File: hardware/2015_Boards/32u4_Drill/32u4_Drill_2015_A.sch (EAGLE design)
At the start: 25 parts, among them U2 XBEE-1B3

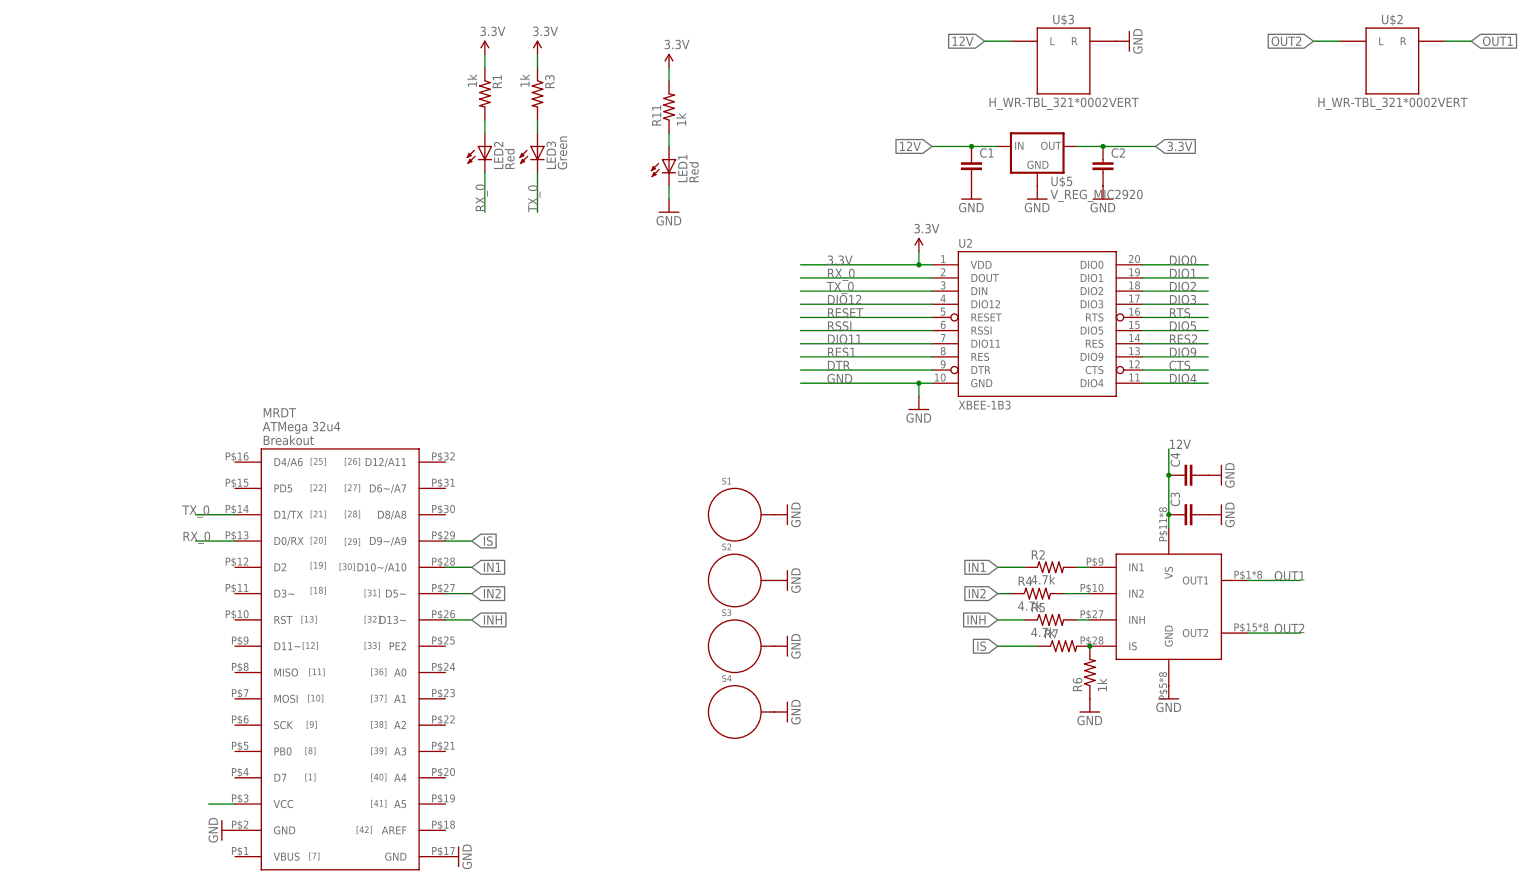
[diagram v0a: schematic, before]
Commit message: Update some Capacitor Values
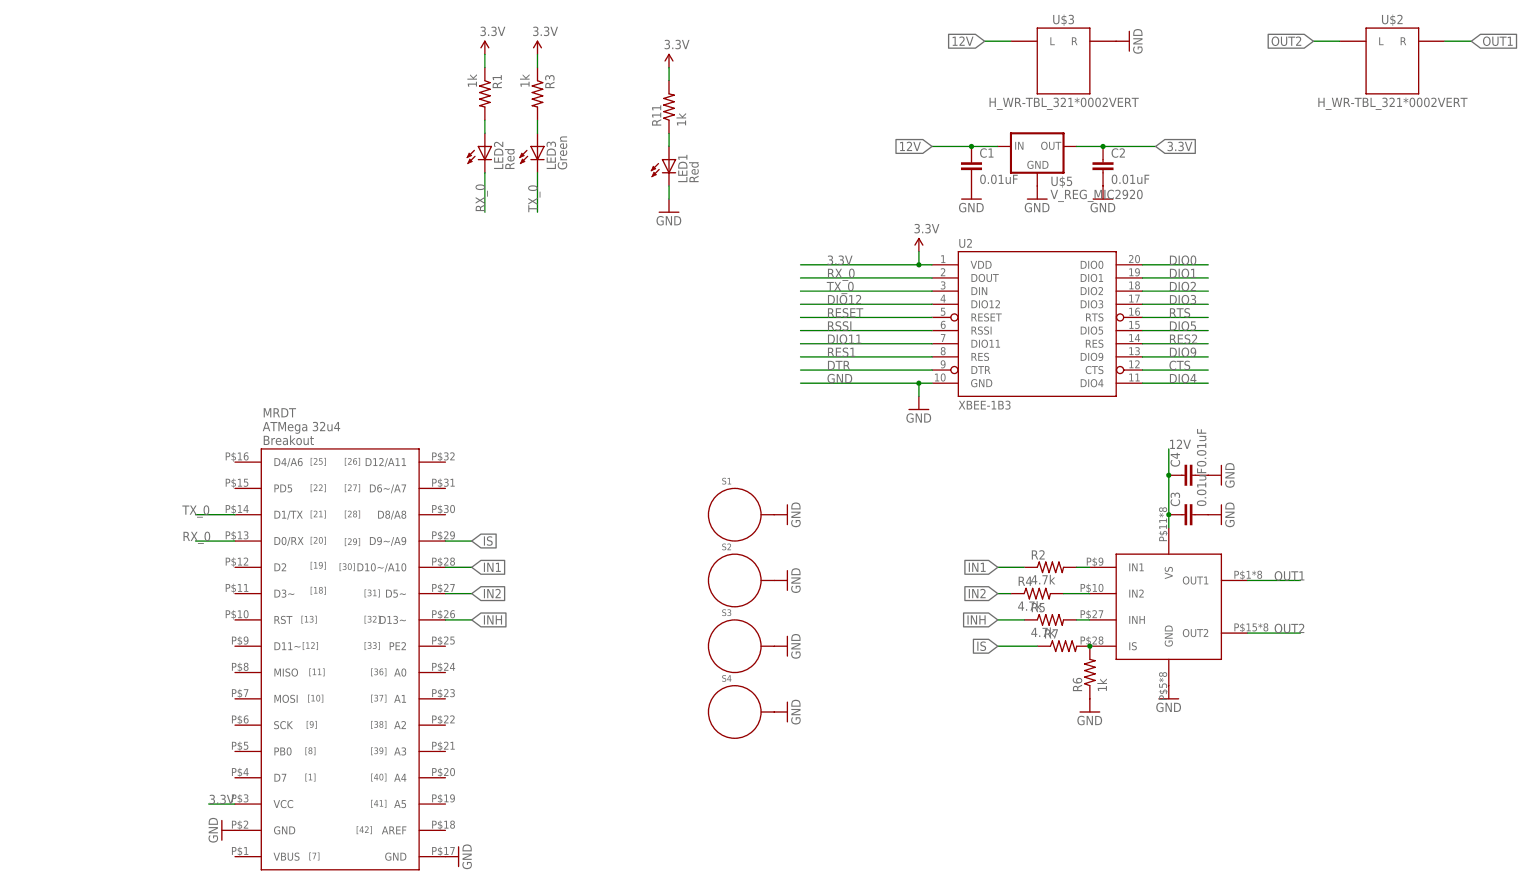
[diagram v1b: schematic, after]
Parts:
- C1, C2, C3, C4: value (none) -> 0.01uF
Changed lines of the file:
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@@
 <?xml version="1.0" encoding="utf-8"?>
 <!DOCTYPE eagle SYSTEM "eagle.dtd">
-<eagle version="6.6.0">
+<eagle version="6.5.0">
 <drawing>
 <settings>
@@
 <part name="U$4" library="MRDT-2015-General" deviceset="BTM7752G" device=""/>
 <part name="GND10" library="SparkFun" deviceset="GND" device=""/>
-<part name="C1" library="SparkFun-Passives" deviceset="CAP" device="1206"/>
-<part name="C2" library="SparkFun-Passives" deviceset="CAP" device="1206"/>
+<part name="C1" library="SparkFun-Passives" deviceset="CAP" device="1206" value="0.01uF"/>
+<part name="C2" library="SparkFun-Passives" deviceset="CAP" device="1206" value="0.01uF"/>
 <part name="GND11" library="SparkFun" deviceset="GND" device=""/>
 <part name="GND12" library="SparkFun" deviceset="GND" device=""/>
@@
 <part name="GND13" library="SparkFun" deviceset="GND" device=""/>
 <part name="R7" library="SparkFun-Passives" deviceset="RESISTOR" device="1206"/>
-<part name="C3" library="SparkFun-Passives" deviceset="CAP" device="1206"/>
-<part name="C4" library="SparkFun-Passives" deviceset="CAP" device="1206"/>
+<part name="C3" library="SparkFun-Passives" deviceset="CAP" device="1206" value="0.01uF"/>
+<part name="C4" library="SparkFun-Passives" deviceset="CAP" device="1206" value="0.01uF"/>
 <part name="GND14" library="SparkFun" deviceset="GND" device=""/>
 <part name="GND15" library="SparkFun" deviceset="GND" device=""/>
@@
 <pinref part="U$1" gate="G$1" pin="VCC"/>
 <wire x1="0" y1="15.24" x2="5.08" y2="15.24" width="0.1524" layer="91"/>
-</segment>
-<segment>
+<label x="0" y="15.24" size="1.778" layer="95"/>
+</segment>
+<segment>

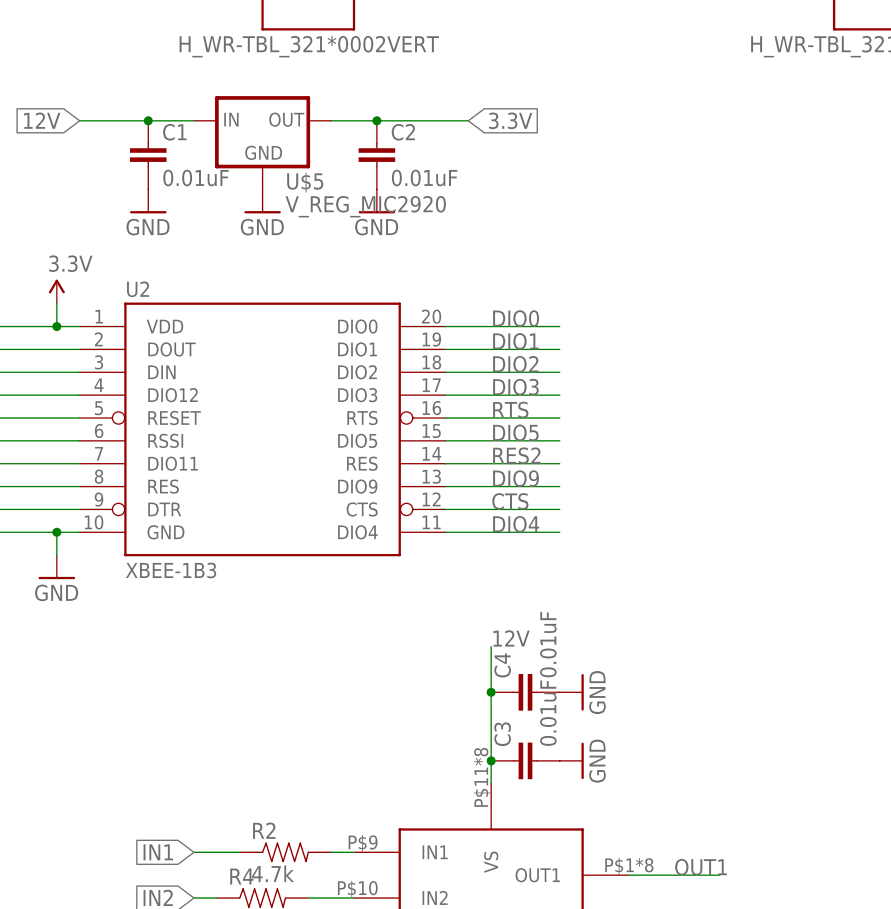
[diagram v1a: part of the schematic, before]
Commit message: Added a beefy capacitor because the datasheet told me too
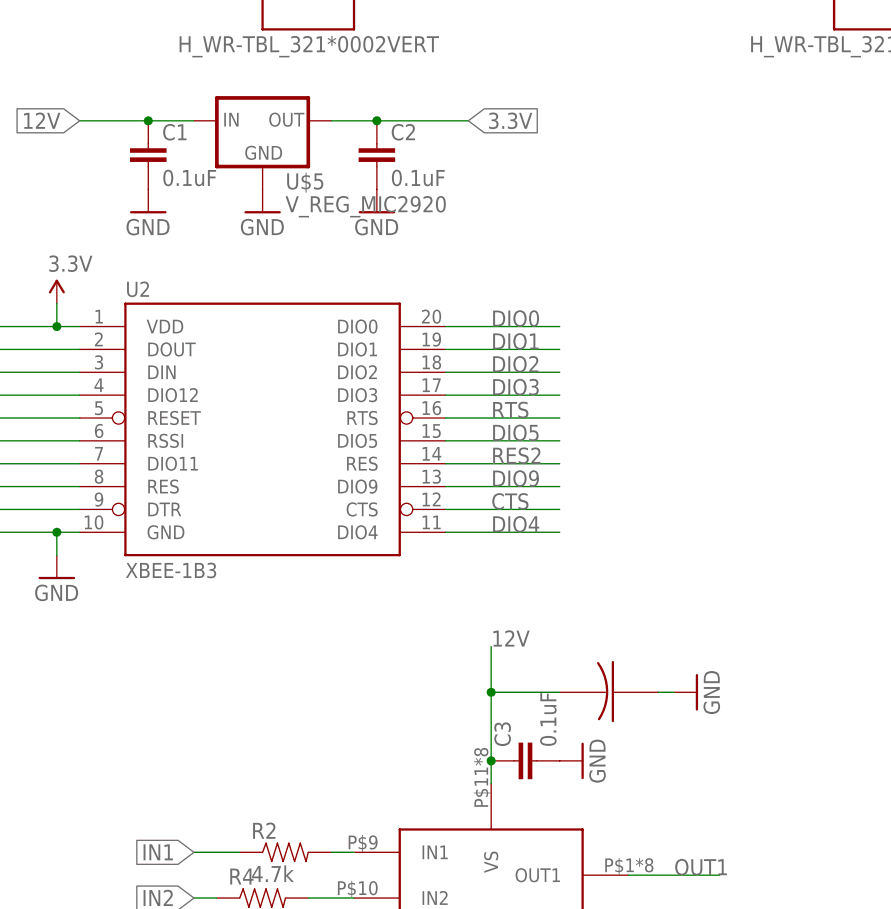
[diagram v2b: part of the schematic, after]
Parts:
- removed C4: 0.01uF, SparkFun-Passives:CAP1206
- added U$6: 100UF-ELECTRO-CAP, New:100UF-ELECTRO-CAP
- C1, C2, C3: value 0.01uF -> 0.1uF
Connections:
- net 12V: now also U$6.POS; no longer C4.1
- net GND: no longer C4.2
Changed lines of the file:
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@@
 <setting verticaltext="up"/>
 </settings>
-<grid distance="0.1" unitdist="inch" unit="inch" style="lines" multiple="1" display="no" altdistance="0.01" altunitdist="inch" altunit="inch"/>
+<grid distance="0.01" unitdist="inch" unit="inch" style="lines" multiple="1" display="no" altdistance="0.01" altunitdist="inch" altunit="inch"/>
 <layers>
 <layer number="1" name="Top" color="4" fill="1" visible="no" active="no"/>
 <layer number="2" name="Route2" color="1" fill="3" visible="no" active="no"/>
+<layer number="3" name="Route3" color="4" fill="3" visible="no" active="no"/>
+<layer number="4" name="Route4" color="1" fill="4" visible="no" active="no"/>
+<layer number="5" name="Route5" color="4" fill="4" visible="no" active="no"/>
+<layer number="6" name="Route6" color="1" fill="8" visible="no" active="no"/>
+<layer number="7" name="Route7" color="4" fill="8" visible="no" active="no"/>
+<layer number="8" name="Route8" color="1" fill="2" visible="no" active="no"/>
+<layer number="9" name="Route9" color="4" fill="2" visible="no" active="no"/>
+<layer number="10" name="Route10" color="1" fill="7" visible="no" active="no"/>
+<layer number="11" name="Route11" color="4" fill="7" visible="no" active="no"/>
+<layer number="12" name="Route12" color="1" fill="5" visible="no" active="no"/>
+<layer number="13" name="Route13" color="4" fill="5" visible="no" active="no"/>
+<layer number="14" name="Route14" color="1" fill="6" visible="no" active="no"/>
 <layer number="15" name="Route15" color="4" fill="6" visible="no" active="no"/>
 <layer number="16" name="Bottom" color="1" fill="1" visible="no" active="no"/>
@@
 <part name="U$4" library="MRDT-2015-General" deviceset="BTM7752G" device=""/>
 <part name="GND10" library="SparkFun" deviceset="GND" device=""/>
-<part name="C1" library="SparkFun-Passives" deviceset="CAP" device="1206" value="0.01uF"/>
-<part name="C2" library="SparkFun-Passives" deviceset="CAP" device="1206" value="0.01uF"/>
+<part name="C1" library="SparkFun-Passives" deviceset="CAP" device="1206" value="0.1uF"/>
+<part name="C2" library="SparkFun-Passives" deviceset="CAP" device="1206" value="0.1uF"/>
 <part name="GND11" library="SparkFun" deviceset="GND" device=""/>
 <part name="GND12" library="SparkFun" deviceset="GND" device=""/>
@@
 <part name="GND13" library="SparkFun" deviceset="GND" device=""/>
 <part name="R7" library="SparkFun-Passives" deviceset="RESISTOR" device="1206"/>
-<part name="C3" library="SparkFun-Passives" deviceset="CAP" device="1206" value="0.01uF"/>
-<part name="C4" library="SparkFun-Passives" deviceset="CAP" device="1206" value="0.01uF"/>
+<part name="C3" library="SparkFun-Passives" deviceset="CAP" device="1206" value="0.1uF"/>
 <part name="GND14" library="SparkFun" deviceset="GND" device=""/>
 <part name="GND15" library="SparkFun" deviceset="GND" device=""/>
+<part name="U$6" library="New" deviceset="100UF-ELECTRO-CAP" device=""/>
 </parts>
 <sheets>
@@
 <instance part="R7" gate="G$1" x="165.1" y="45.72"/>
 <instance part="C3" gate="G$1" x="190.5" y="71.12" rot="R90"/>
-<instance part="C4" gate="G$1" x="190.5" y="78.74" rot="R90"/>
-<instance part="GND14" gate="1" x="195.58" y="78.74" rot="R90"/>
+<instance part="GND14" gate="1" x="208.28" y="78.74" rot="R90"/>
 <instance part="GND15" gate="1" x="195.58" y="71.12" rot="R90"/>
+<instance part="U$6" gate="G$1" x="220.98" y="66.04"/>
 </instances>
 <busses>
@@
 </segment>
 <segment>
-<pinref part="C4" gate="G$1" pin="2"/>
-<pinref part="GND14" gate="1" pin="GND"/>
-</segment>
-<segment>
 <pinref part="C3" gate="G$1" pin="2"/>
 <pinref part="GND15" gate="1" pin="GND"/>
+</segment>
+<segment>
+<pinref part="GND14" gate="1" pin="GND"/>
+<wire x1="205.74" y1="78.74" x2="203.962" y2="78.74" width="0.1524" layer="91"/>
 </segment>
 </net>
@@
 <wire x1="185.42" y1="71.12" x2="185.42" y2="78.74" width="0.1524" layer="91"/>
 <junction x="185.42" y="71.12"/>
-<pinref part="C4" gate="G$1" pin="1"/>
+<pinref part="U$6" gate="G$1" pin="POS"/>
 <wire x1="185.42" y1="78.74" x2="185.42" y2="83.82" width="0.1524" layer="91"/>
+<wire x1="193.04" y1="78.74" x2="185.42" y2="78.74" width="0.1524" layer="91"/>
 <junction x="185.42" y="78.74"/>
 </segment>

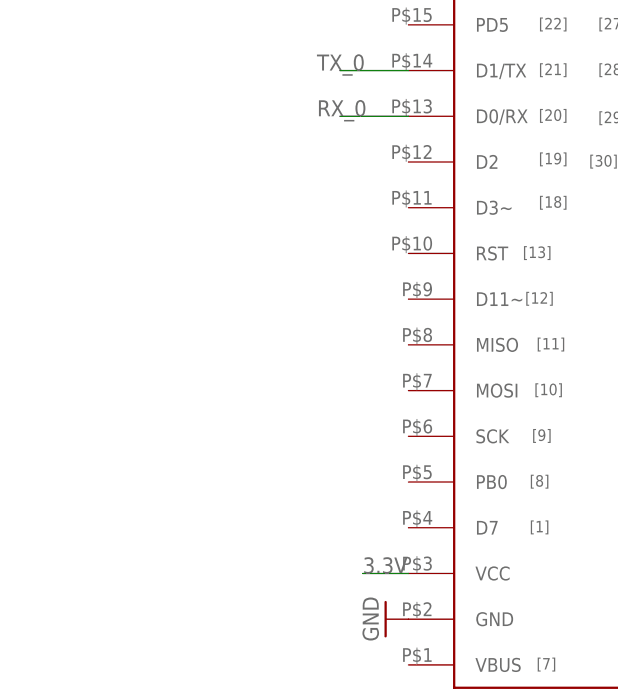
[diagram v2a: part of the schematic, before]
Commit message: Added sensor breakouts for forgotten sensors
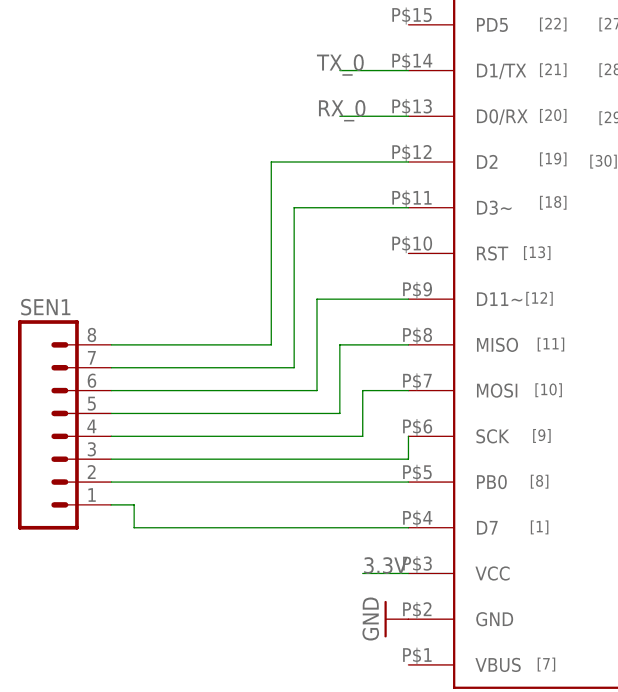
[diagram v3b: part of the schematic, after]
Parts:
- added SEN1: (no value), SparkFun-Connectors:M081X08
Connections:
- new net N$10: SEN1.4, U$1.MOSI
- new net N$11: SEN1.5, U$1.MISO
- new net N$12: SEN1.6, U$1.D11~
- new net N$13: SEN1.7, U$1.D3~
- new net N$14: SEN1.8, U$1.D2
- new net N$7: SEN1.1, U$1.D7
- new net N$8: SEN1.2, U$1.PB0
- new net N$9: SEN1.3, U$1.SCK
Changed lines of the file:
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@@
 <setting verticaltext="up"/>
 </settings>
-<grid distance="0.01" unitdist="inch" unit="inch" style="lines" multiple="1" display="no" altdistance="0.01" altunitdist="inch" altunit="inch"/>
+<grid distance="0.1" unitdist="inch" unit="inch" style="lines" multiple="1" display="no" altdistance="0.01" altunitdist="inch" altunit="inch"/>
 <layers>
 <layer number="1" name="Top" color="4" fill="1" visible="no" active="no"/>
@@
 <part name="GND15" library="SparkFun" deviceset="GND" device=""/>
 <part name="U$6" library="New" deviceset="100UF-ELECTRO-CAP" device=""/>
+<part name="SEN1" library="SparkFun-Connectors" deviceset="M08" device="1X08"/>
 </parts>
 <sheets>
@@
 <instance part="GND15" gate="1" x="195.58" y="71.12" rot="R90"/>
 <instance part="U$6" gate="G$1" x="220.98" y="66.04"/>
+<instance part="SEN1" gate="G$1" x="-33.02" y="30.48"/>
 </instances>
 <busses>
@@
 </segment>
 </net>
+<net name="N$7" class="0">
+<segment>
+<pinref part="U$1" gate="G$1" pin="D7"/>
+<wire x1="5.08" y1="20.32" x2="-25.4" y2="20.32" width="0.1524" layer="91"/>
+<pinref part="SEN1" gate="G$1" pin="1"/>
+<wire x1="-25.4" y1="20.32" x2="-25.4" y2="22.86" width="0.1524" layer="91"/>
+<wire x1="-25.4" y1="22.86" x2="-27.94" y2="22.86" width="0.1524" layer="91"/>
+</segment>
+</net>
+<net name="N$8" class="0">
+<segment>
+<pinref part="U$1" gate="G$1" pin="PB0"/>
+<pinref part="SEN1" gate="G$1" pin="2"/>
+<wire x1="5.08" y1="25.4" x2="-27.94" y2="25.4" width="0.1524" layer="91"/>
+</segment>
+</net>
+<net name="N$9" class="0">
+<segment>
+<pinref part="U$1" gate="G$1" pin="SCK"/>
+<pinref part="SEN1" gate="G$1" pin="3"/>
+<wire x1="5.08" y1="30.48" x2="5.08" y2="27.94" width="0.1524" layer="91"/>
+<wire x1="5.08" y1="27.94" x2="-27.94" y2="27.94" width="0.1524" layer="91"/>
+</segment>
+</net>
+<net name="N$10" class="0">
+<segment>
+<pinref part="U$1" gate="G$1" pin="MOSI"/>
+<wire x1="5.08" y1="35.56" x2="0" y2="35.56" width="0.1524" layer="91"/>
+<wire x1="0" y1="35.56" x2="0" y2="30.48" width="0.1524" layer="91"/>
+<pinref part="SEN1" gate="G$1" pin="4"/>
+<wire x1="0" y1="30.48" x2="-27.94" y2="30.48" width="0.1524" layer="91"/>
+</segment>
+</net>
+<net name="N$11" class="0">
+<segment>
+<pinref part="U$1" gate="G$1" pin="MISO"/>
+<wire x1="5.08" y1="40.64" x2="-2.54" y2="40.64" width="0.1524" layer="91"/>
+<wire x1="-2.54" y1="40.64" x2="-2.54" y2="33.02" width="0.1524" layer="91"/>
+<pinref part="SEN1" gate="G$1" pin="5"/>
+<wire x1="-2.54" y1="33.02" x2="-27.94" y2="33.02" width="0.1524" layer="91"/>
+</segment>
+</net>
+<net name="N$12" class="0">
+<segment>
+<pinref part="U$1" gate="G$1" pin="D11~"/>
+<wire x1="5.08" y1="45.72" x2="-5.08" y2="45.72" width="0.1524" layer="91"/>
+<wire x1="-5.08" y1="45.72" x2="-5.08" y2="35.56" width="0.1524" layer="91"/>
+<pinref part="SEN1" gate="G$1" pin="6"/>
+<wire x1="-5.08" y1="35.56" x2="-27.94" y2="35.56" width="0.1524" layer="91"/>
+</segment>
+</net>
+<net name="N$13" class="0">
+<segment>
+<pinref part="U$1" gate="G$1" pin="D3~"/>
+<wire x1="5.08" y1="55.88" x2="-7.62" y2="55.88" width="0.1524" layer="91"/>
+<pinref part="SEN1" gate="G$1" pin="7"/>
+<wire x1="-7.62" y1="55.88" x2="-7.62" y2="38.1" width="0.1524" layer="91"/>
+<wire x1="-7.62" y1="38.1" x2="-27.94" y2="38.1" width="0.1524" layer="91"/>
+</segment>
+</net>
+<net name="N$14" class="0">
+<segment>
+<pinref part="U$1" gate="G$1" pin="D2"/>
+<wire x1="5.08" y1="60.96" x2="-10.16" y2="60.96" width="0.1524" layer="91"/>
+<pinref part="SEN1" gate="G$1" pin="8"/>
+<wire x1="-10.16" y1="60.96" x2="-10.16" y2="40.64" width="0.1524" layer="91"/>
+<wire x1="-10.16" y1="40.64" x2="-27.94" y2="40.64" width="0.1524" layer="91"/>
+</segment>
+</net>
